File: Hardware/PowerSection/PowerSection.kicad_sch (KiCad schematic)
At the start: 35 parts, among them J1 Conn_01x05_Male, J2 Conn_01x02_Pin, Q1 T2N7002AK,LM, U1 INA180B4, U2 INA180B1, U4 ZXGD3009DY

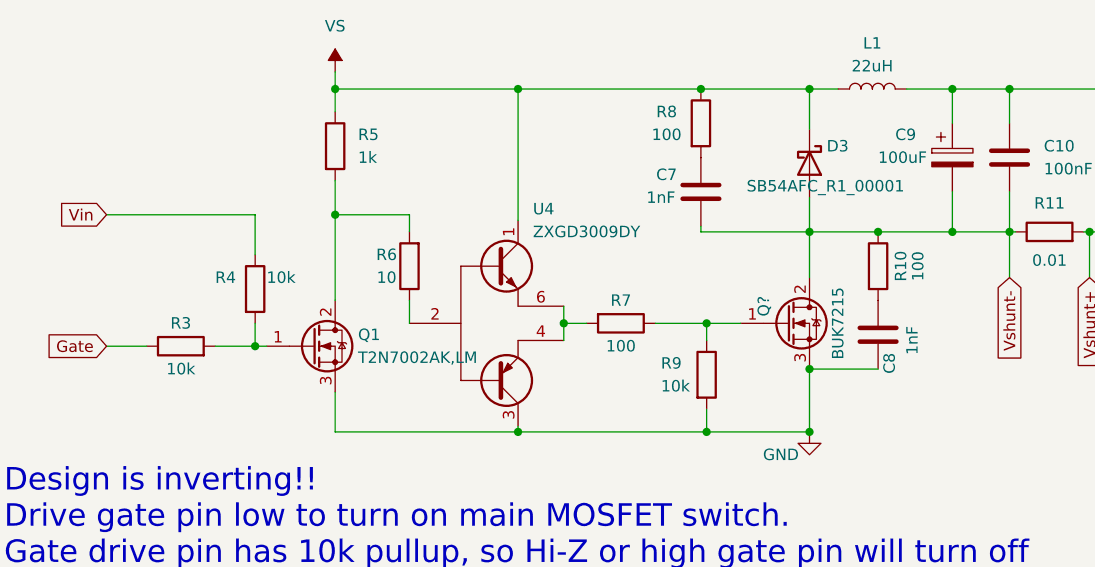
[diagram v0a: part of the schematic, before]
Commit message: Annotated some parts with LCSC and Digikey part numbers. Updated spice model to match reference designators in the Kicad schematic.
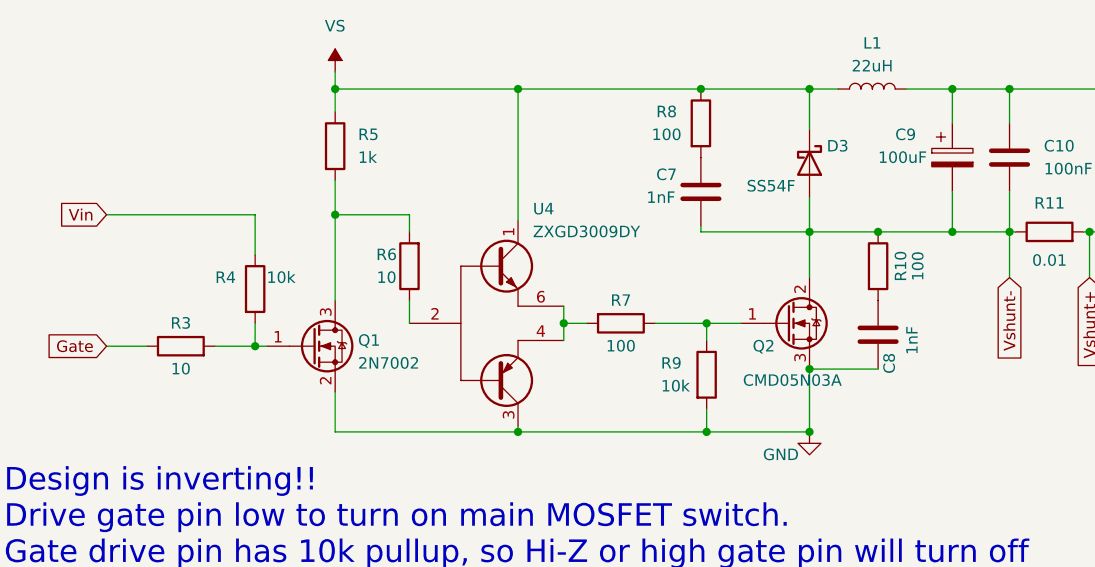
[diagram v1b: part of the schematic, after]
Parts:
- removed Q1: T2N7002AK,LM, Package_TO_SOT_SMD:SOT-23, symbol Transistor_FET:QM6006D
- added Q1: 2N7002, Package_TO_SOT_SMD:SOT-23, symbol Transistor_FET:2N7002
- D3: value SB54AFC_R1_00001 -> SS54F; footprint Brett-Footprint:DO221AC -> Brett-Footprint:D_SMAF; Digikey Part (none) -> 3757-SB54AFC_R1_00001CT-ND; LCSC Part (none) -> C915624
- Q2: renamed from Q?; value BUK7215 -> CMD05N03A; Digikey Part (none) -> 353-MCU80N03A-TPCT-ND; LCSC Part (none) -> C5203816
- R3: value 10k -> 10
- U1: Digikey Part (none) -> 296-INA180B4IDBVRCT-ND; LCSC Part (none) -> C1879708
- U2: Digikey Part (none) -> 296-48130-1-ND; LCSC Part (none) -> C544664
- U4: Digikey Part (none) -> ZXGD3009DYTADICT-ND; LCSC Part (none) -> C441818
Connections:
- net GND: now also Q1.2 (S)
- net at R5.2, R6.2: now also Q1.3 (D)
- net at R3.2, R4.2: now also Q1.1 (G)

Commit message: Replaced custom global symbols with standard KiCad symbols or local project symbols.
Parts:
- Q2: symbol Brett_sym:BUK7215 -> Transistor_FET:IPD50R380CE
- U1, U2: symbol Brett-7.0:INA180Bx -> PowerSection:INA180Bx
- U4: symbol Brett-7.0:ZXGD3009DY -> PowerSection:ZXGD3009DY
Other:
- title: (none) -> Modular Solder Reflow Power Section
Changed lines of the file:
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@@
 (kicad_sch (version 20230121) (generator eeschema)
-  (paper "A4")
+  (paper "USLetter")
+  (title_block
+    (title "Modular Solder Reflow Power Section")
+    (date "2023-04-26")
+    (rev "0.0")
+  )
   (junction (at 144.78 31.75) (diameter 0) (color 0 0 0 0)
   )
@@
     )
   )
-  (symbol (lib_id "Brett_sym:BUK7215") (at 194.945 57.785 0) (unit 1)
+  (symbol (lib_id "Transistor_FET:IPD50R380CE") (at 194.945 57.785 0) (unit 1)
     (in_bom yes) (on_board yes) (dnp no)
     (property "Reference" "Q2" (at 192.405 60.325 0)
@@
       (effects (font (size 1.27 1.27) italic) (justify left) hide)
     )
-    (property "Datasheet" "https://datasheet.lcsc.com/lcsc/2210191430_Cmos-CMD05N03A_C5203816.pdf" (at 194.945 57.785 0)
+    (property "Datasheet" "https://www.infineon.com/dgdl/Infineon-IPD50R380CE-DS-v02_01-en.pdf?fileId=db3a30433ecb86d4013ed0a2ef580f38" (at 194.945 57.785 0)
       (effects (font (size 1.27 1.27)) (justify left) hide)
     )
@@
     )
   )
-  (symbol (lib_id "Brett-7.0:INA180Bx") (at 46.355 129.54 0) (mirror y) (unit 1)
+  (symbol (lib_id "PowerSection:INA180Bx") (at 46.355 129.54 0) (mirror y) (unit 1)
     (in_bom yes) (on_board yes) (dnp no)
     (property "Reference" "U2" (at 45.085 123.19 0)
@@
     )
   )
-  (symbol (lib_id "Brett-7.0:ZXGD3009DY") (at 162.56 57.785 0) (unit 1)
+  (symbol (lib_id "PowerSection:ZXGD3009DY") (at 162.56 57.785 0) (unit 1)
     (in_bom yes) (on_board yes) (dnp no) (fields_autoplaced)
     (property "Reference" "U4" (at 166.7511 45.085 0)
@@
     )
   )
-  (symbol (lib_id "Brett-7.0:INA180Bx") (at 70.485 129.54 0) (unit 1)
+  (symbol (lib_id "PowerSection:INA180Bx") (at 70.485 129.54 0) (unit 1)
     (in_bom yes) (on_board yes) (dnp no)
     (property "Reference" "U1" (at 70.485 121.92 0)

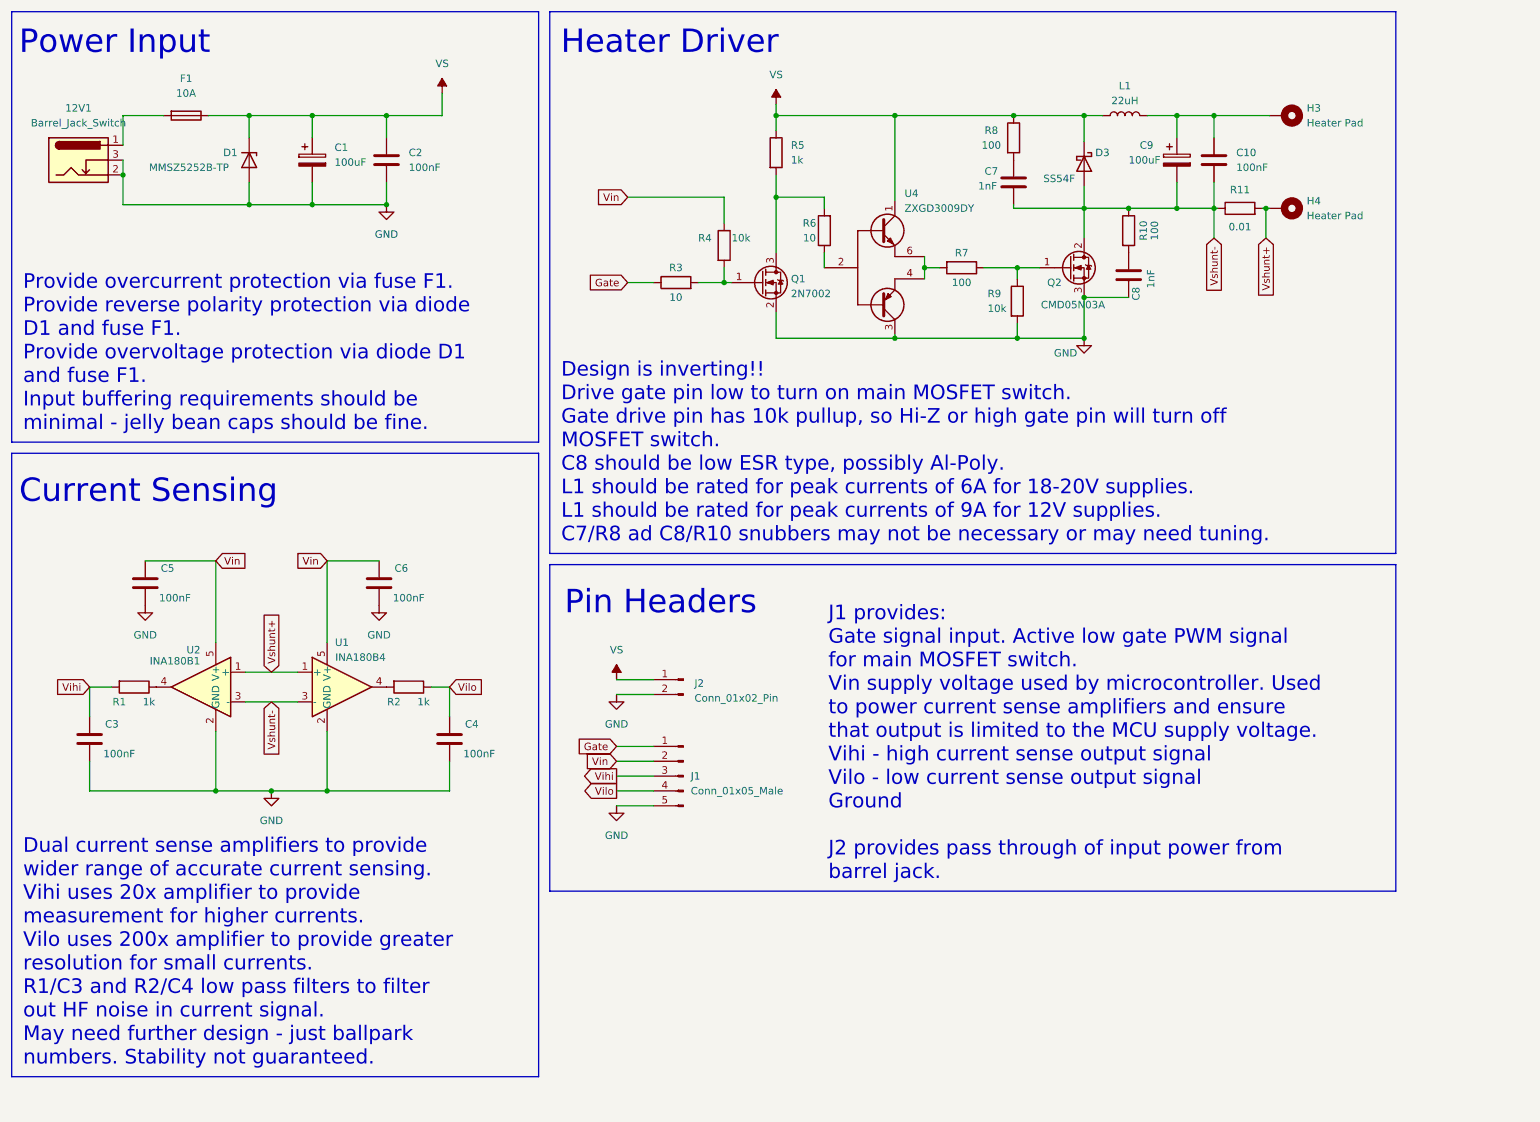
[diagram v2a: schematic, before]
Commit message: Updated footprints to use standard or project local footprints. Updated component specs to handle 12V 100W hotplates - beefier inductors. Added input ripple filter inductor.
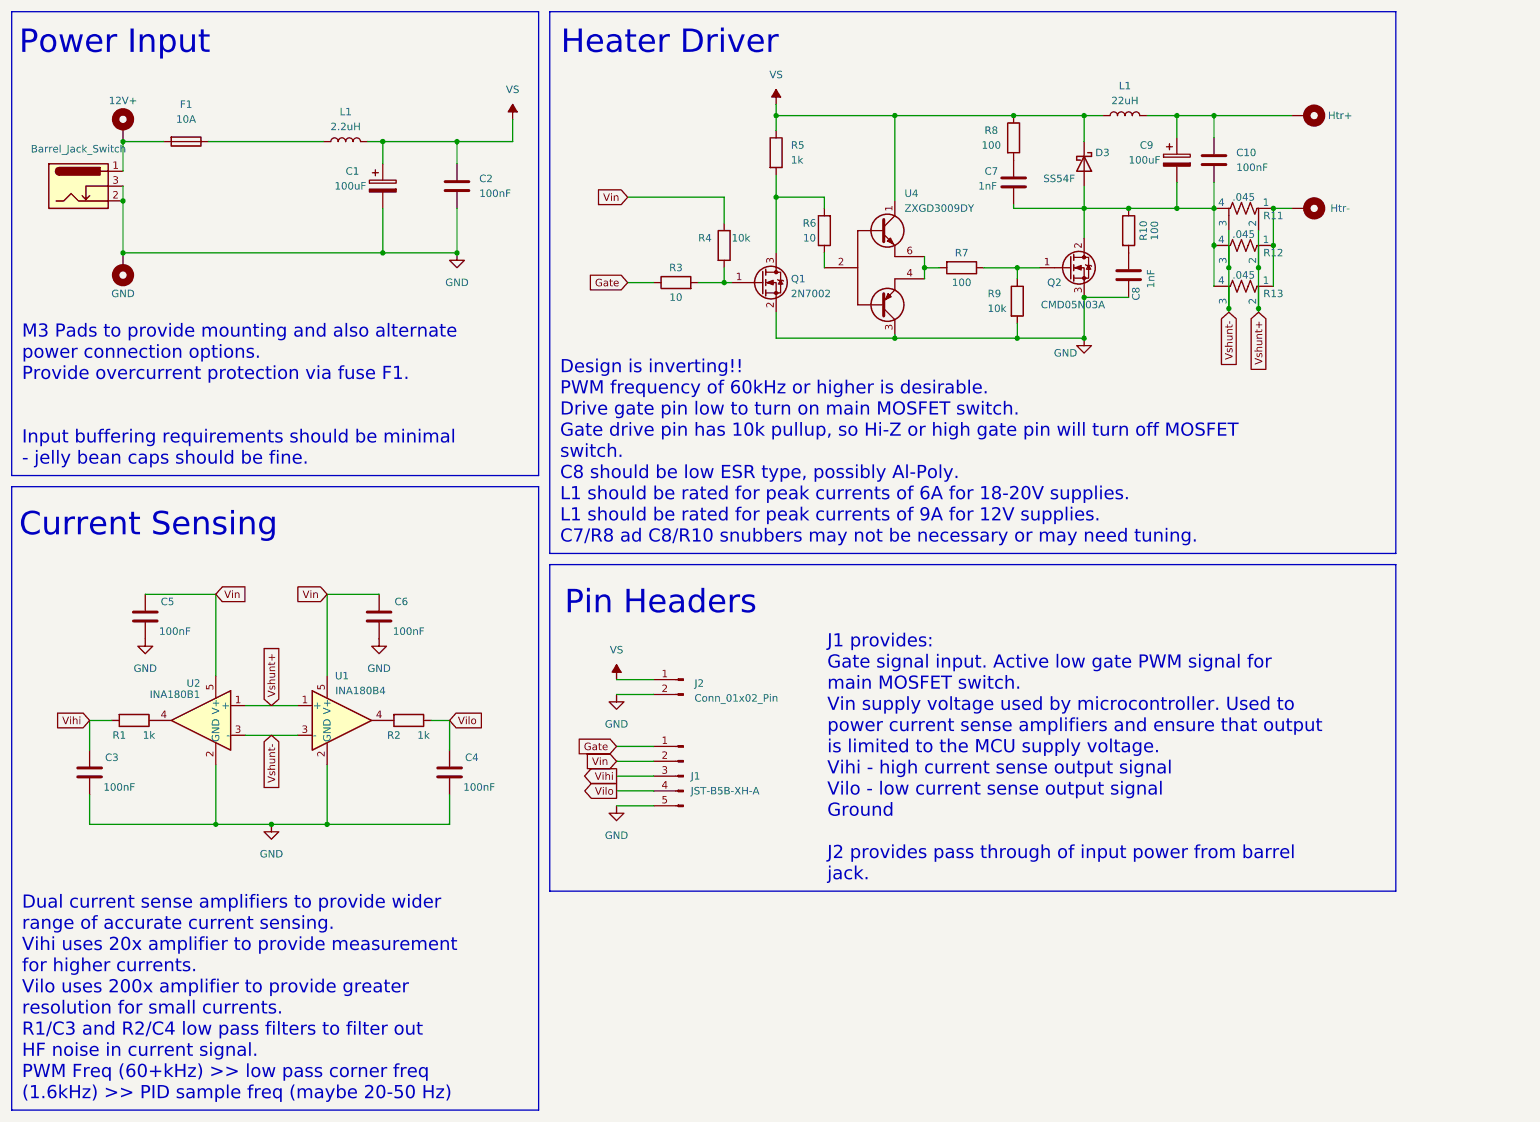
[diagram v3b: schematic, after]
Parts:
- removed D1: MMSZ5252B-TP, Diode_SMD:D_SOD-123F, symbol Diode:BZT52Bxx
- removed R11: 0.01, Brett-Footprint:R_2512_Shunt, symbol Device:R
- added H2, H5: MountingHole_Pad, symbol Mechanical:MountingHole_Pad
- added L1: 2.2uH, PowerSection:L_12x12-ish, symbol Device:L
- added R11, R12, R13: .045, PowerSection:R_2512_Kelvin_Shunt, symbol Device:R_Shunt_US
- 12V1: Digikey Part (none) -> 839-54-00167-ND; LCSC Part (none) -> C5155560
- C1, C9: Digikey Part (none) -> 399-A768KE107M1VLAE036CT-ND; LCSC Part (none) -> C454651
- D3: footprint Brett-Footprint:D_SMAF -> PowerSection:D_SMBF; Digikey Part 3757-SB54AFC_R1_00001CT-ND -> 3757-STR8100LBF_R1_00701CT-ND; LCSC Part C915624 -> C2922187
- F1: footprint Brett-Footprint:R_1206_Fuse -> PowerSection:R_1206_Fuse; Digikey Part (none) -> 507-1942-1-ND; LCSC Part (none) -> C207003
- H3: Name (none) -> Htr+
- H4: Name (none) -> Htr-
- J1: value Conn_01x05_Male -> JST-B5B-XH-A; footprint Connector_PinHeader_2.54mm:PinHeader_1x05_P2.54mm_Vertical -> Connector_JST:JST_XH_B5B-XH-A_1x05_P2.50mm_Vertical; Digikey Part (none) -> 1175-51025-06-0100-01-ND; LCSC Part (none) -> C722877
- J2: footprint (none) -> Connector_PinHeader_2.54mm:PinHeader_1x02_P2.54mm_Vertical; Digikey Part (none) -> S1011EC-02-ND; LCSC Part (none) -> C2894925
- L1: footprint Brett-Footprint:L_Bourns_SRP1265c -> PowerSection:L_25x15_FlatWire; Digikey Part (none) -> PQ2617BHA-220K-ND; LCSC Part (none) -> C2761965
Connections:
- net GND: now also H5.1
- net VS: now also L1.2; no longer F1.1
- net Vshunt+: now also R11.2, R12.2, R13.2; no longer H4.1
- net Vshunt-: now also R11.3, R12.3, R13.3; no longer C10.2, C7.2, C9.2, D3.2 (A), Q2.2 (D), R10.1
- net at 12V1.1, F1.2: now also H2.1
- new net: C10.2, C7.2, C9.2, D3.2 (A), Q2.2 (D), R10.1, R11.4, R12.4, R13.4
- new net: H4.1, R11.1, R12.1, R13.1
- new net: F1.1, L1.1
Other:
- moved on the sheet: C2, C3, C4, C5, C6, F1, R1, R2, U1, U2

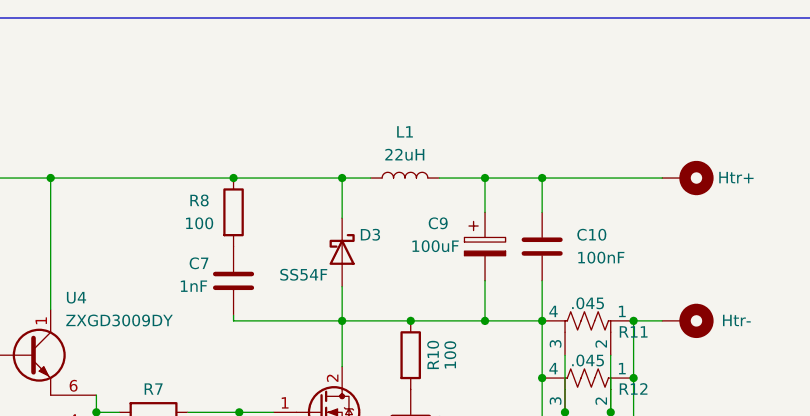
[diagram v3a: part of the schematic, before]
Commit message: Fixed inductor reference designators on PowerSection design.
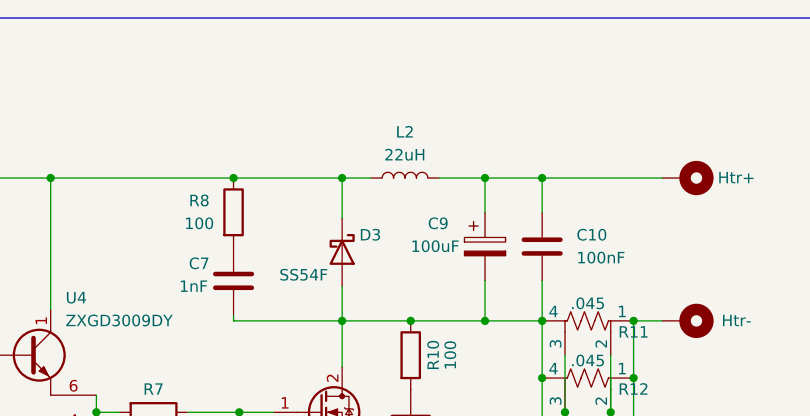
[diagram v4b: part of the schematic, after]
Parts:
- renumbered L1 to L2
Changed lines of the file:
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@@
   (symbol (lib_id "Device:L") (at 204.47 31.75 90) (unit 1)
     (in_bom yes) (on_board yes) (dnp no) (fields_autoplaced)
-    (property "Reference" "L1" (at 204.47 26.67 90)
+    (property "Reference" "L2" (at 204.47 26.67 90)
       (effects (font (size 1.27 1.27)))
     )
@@
       (project "PowerSection"
         (path "/d77f81f5-4aeb-4219-833e-6d0cccd39831"
-          (reference "L1") (unit 1)
+          (reference "L2") (unit 1)
         )
       )
